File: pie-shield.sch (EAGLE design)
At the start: 15 parts, among them IC6 78L05, IC8 MAX487, X6 RJ45-8L-B

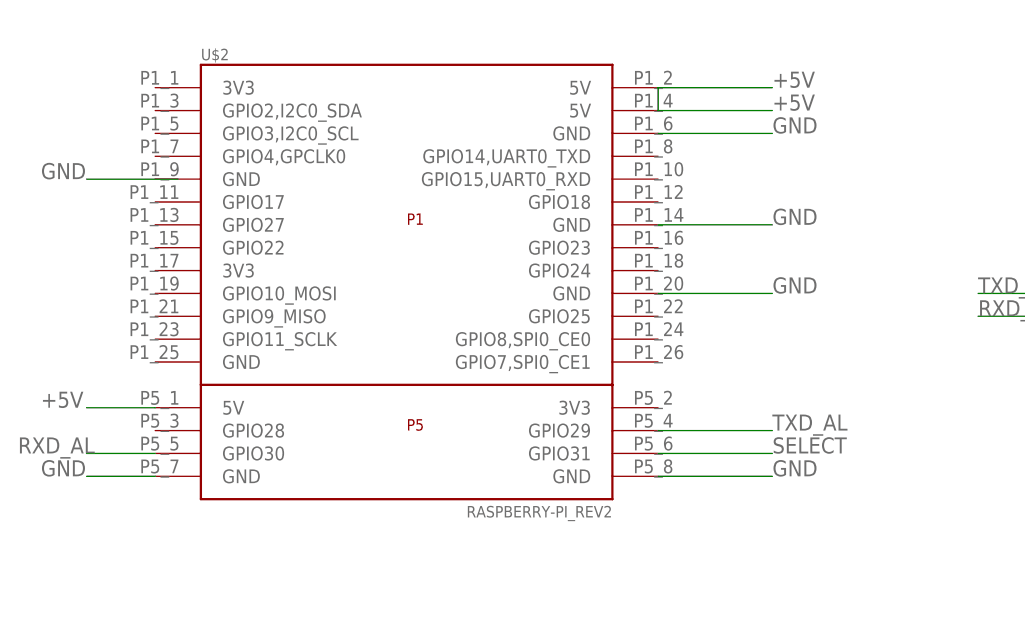
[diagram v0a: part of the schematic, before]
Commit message: using uart pins
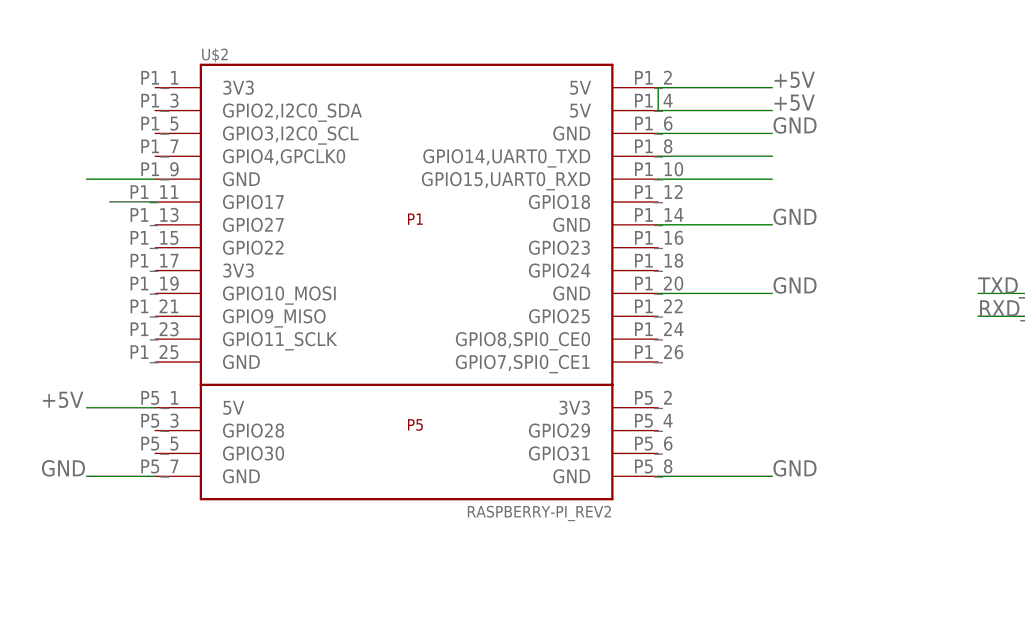
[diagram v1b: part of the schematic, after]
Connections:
- net GND: now also U$2.GND@9
- net RXD_AL: now also U$2.GPIO15,UART0_RXD; no longer U$2.GPIO30
- net SELECT: now also U$2.GPIO17; no longer U$2.GPIO31
- net TXD_AL: now also U$2.GPIO14,UART0_TXD; no longer U$2.GPIO29
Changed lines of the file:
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@@
 </segment>
 <segment>
-<pinref part="U$2" gate="G$1" pin="GPIO30"/>
-<wire x1="-142.24" y1="33.02" x2="-149.86" y2="33.02" width="0.1524" layer="91"/>
-<label x="-157.48" y="33.02" size="1.778" layer="95"/>
+<pinref part="U$2" gate="G$1" pin="GPIO15,UART0_RXD"/>
+<wire x1="-86.36" y1="63.5" x2="-73.66" y2="63.5" width="0.1524" layer="91"/>
 </segment>
 </net>
@@
 </segment>
 <segment>
-<pinref part="U$2" gate="G$1" pin="GPIO29"/>
-<wire x1="-86.36" y1="35.56" x2="-73.66" y2="35.56" width="0.1524" layer="91"/>
-<label x="-73.66" y="35.56" size="1.778" layer="95"/>
+<pinref part="U$2" gate="G$1" pin="GPIO14,UART0_TXD"/>
+<wire x1="-86.36" y1="66.04" x2="-73.66" y2="66.04" width="0.1524" layer="91"/>
 </segment>
 </net>
@@
 </segment>
 <segment>
-<pinref part="U$2" gate="G$1" pin="GPIO31"/>
-<wire x1="-86.36" y1="33.02" x2="-73.66" y2="33.02" width="0.1524" layer="91"/>
-<label x="-73.66" y="33.02" size="1.778" layer="95"/>
+<pinref part="U$2" gate="G$1" pin="GPIO17"/>
+<wire x1="-142.24" y1="60.96" x2="-147.32" y2="60.96" width="0.1524" layer="91"/>
 </segment>
 </net>
@@
 </segment>
 <segment>
-<wire x1="-139.7" y1="63.5" x2="-149.86" y2="63.5" width="0.1524" layer="91"/>
-<label x="-154.94" y="63.5" size="1.778" layer="95"/>
-</segment>
-<segment>
 <pinref part="U$2" gate="G$1" pin="GND@P5_7"/>
 <wire x1="-142.24" y1="30.48" x2="-149.86" y2="30.48" width="0.1524" layer="91"/>
@@
 <label x="-73.66" y="68.58" size="1.778" layer="95"/>
 </segment>
+<segment>
+<pinref part="U$2" gate="G$1" pin="GND@9"/>
+<wire x1="-142.24" y1="63.5" x2="-149.86" y2="63.5" width="0.1524" layer="91"/>
+</segment>
 </net>
